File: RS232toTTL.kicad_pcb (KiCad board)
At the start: 2 copper layers, 48.5 x 32.5 mm, 15 parts, among them J1 DB9, P1 CONN_01X04, Q1 2N7002, Q2 PNP-BC857

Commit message: Routing PCB
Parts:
- moved R6 20.9 mm to (141.0, 103.5), turned to 180 degrees
- moved R7 19.1 mm to (141.0, 99.5), turned to 180 degrees
- moved D2 16.1 mm to (148.0, 103.5), turned to 180 degrees
- moved R2 15.7 mm to (138.0, 78.5), turned to 0 degrees
- moved R1 12.5 mm to (133.5, 78.5)
- moved D3 9.72 mm to (148.0, 99.5), turned to 180 degrees
- moved C1 7.28 mm to (137.5, 88.0), turned to 180 degrees
- moved P1 6.00 mm to (151.0, 88.0)
- moved D1 5.51 mm to (135.5, 82.0)
- moved Q1 5.45 mm to (145.9, 92.0), turned to 270 degrees
- moved Q2 4.61 mm to (133.5, 98.0)
- moved R5 4.00 mm to (133.5, 103.5), turned to 180 degrees
- moved R3 2.69 mm to (141.0, 96.5), turned to 0 degrees
- moved R4 2.06 mm to (134.0, 94.0)
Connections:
- P1 pad 1: VCC -> GND
- P1 pad 2: Net-(D2-Pad1) -> Net-(D3-Pad1)
- P1 pad 3: Net-(D3-Pad1) -> Net-(D2-Pad1)
- P1 pad 4: GND -> VCC
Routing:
- net Net-(D2-Pad1): track 0.00 -> 34.1 mm
- net VCC: track 0.00 -> 28.8 mm
- net Net-(D3-Pad1): track 0.00 -> 18.9 mm
- net Net-(Q1-Pad1): track 2.50 -> 19.8 mm
- net GND: track 0.00 -> 10.8 mm, vias 0 -> 2
- net Net-(Q2-Pad1): track 0.00 -> 10.5 mm, vias 0 -> 2
- net Net-(D1-Pad1): track 8.39 -> 16.9 mm
- net Net-(D3-Pad2): track 0.00 -> 5.10 mm
- net Net-(D2-Pad2): track 0.00 -> 5.10 mm
- net Net-(J1-Pad2): track 4.96 -> 9.42 mm
- net Net-(C1-Pad2): track 16.8 -> 13.6 mm
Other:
- board size 48.5 x 32.5 mm -> 43.5 x 32.5 mm
- net class 1mm added: clearance 0.3, trace_width 1, via_dia 2, via_drill 1
- net class Default: clearance 0.3 -> 0.5; via_dia 0.6 -> 2; via_drill 0.4 -> 1
- rule trace_clearance: 0.3 -> 0.5

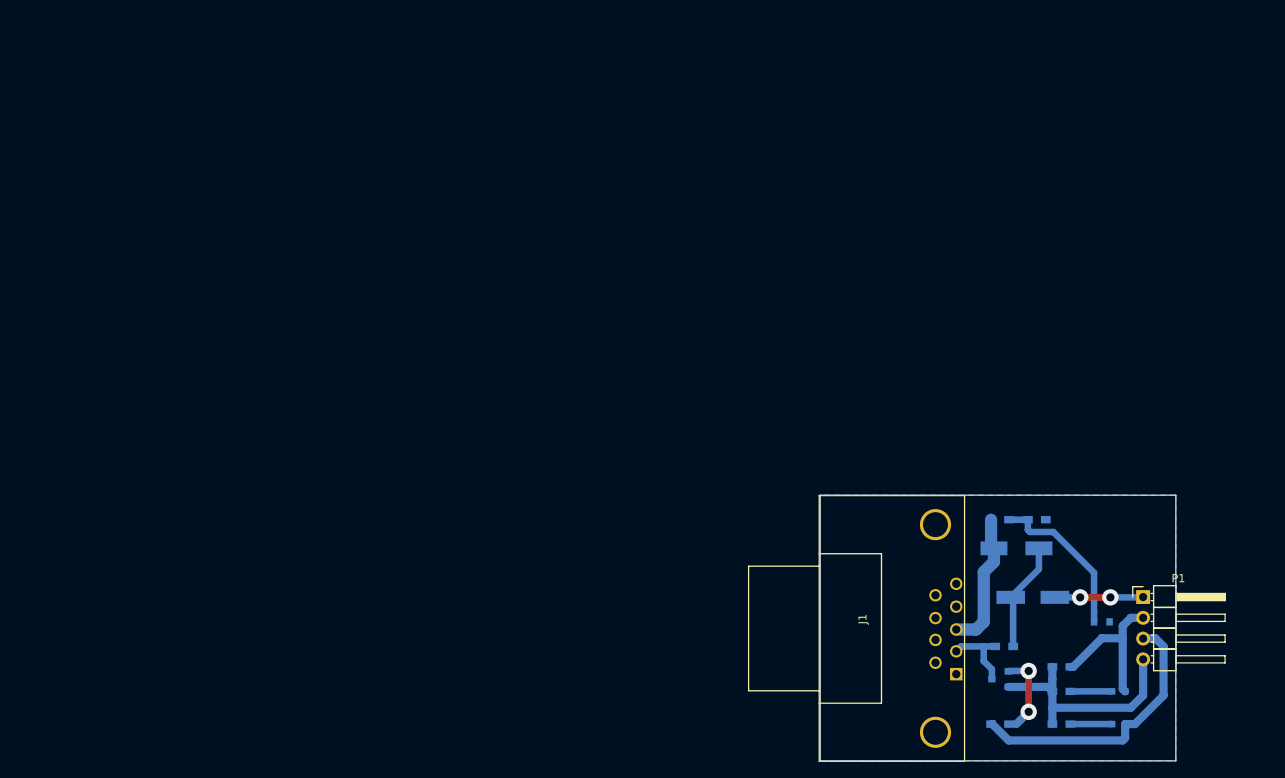
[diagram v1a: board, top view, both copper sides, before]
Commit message: Finalizing the PCB, first print successful
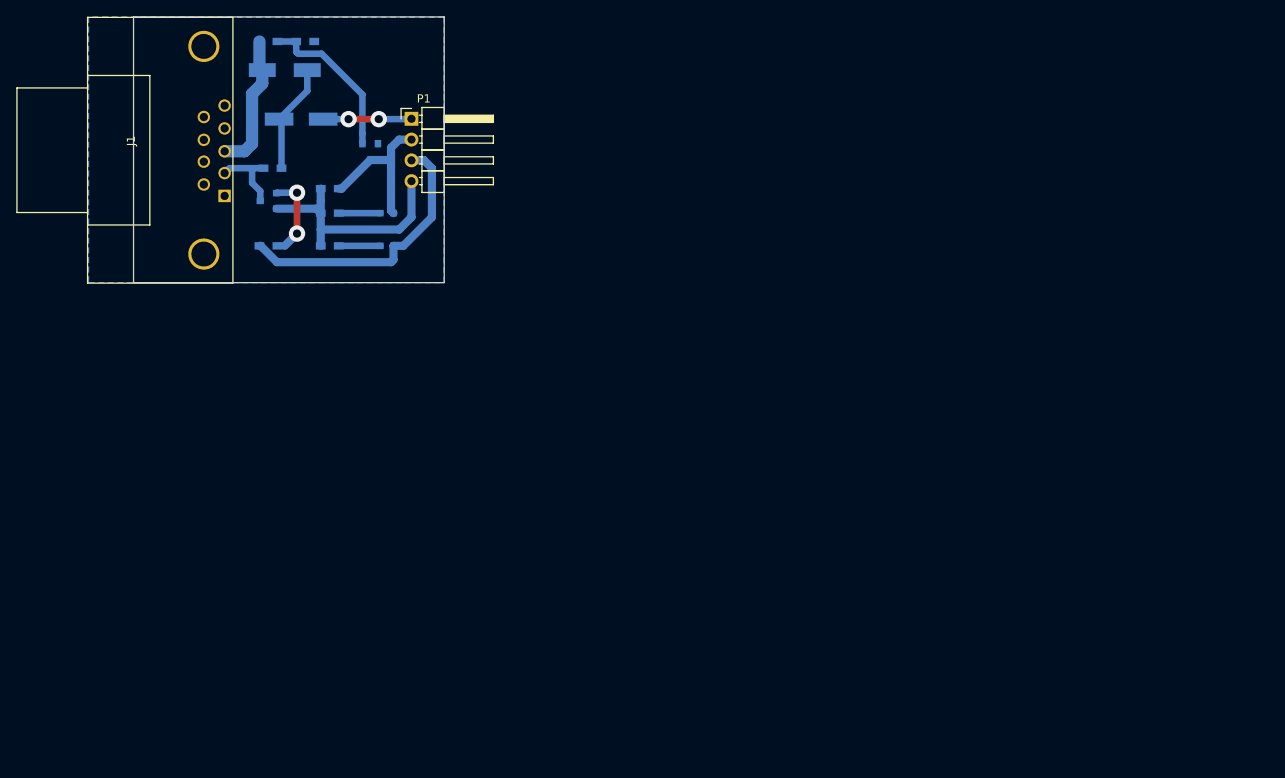
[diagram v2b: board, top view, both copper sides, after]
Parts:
- moved C1 106.9 mm to (48.0, 29.5)
- moved D1 106.9 mm to (46.0, 23.5)
- moved D2 106.9 mm to (58.5, 45.0)
- moved D3 106.9 mm to (58.5, 41.0)
- moved J1 106.9 mm to (37.4, 33.4)
- moved P1 106.9 mm to (61.5, 29.5)
- moved Q1 106.9 mm to (56.5, 33.5)
- moved Q2 106.9 mm to (44.0, 39.5)
- moved R1 106.9 mm to (44.0, 20.0)
- moved R2 106.9 mm to (48.5, 20.0)
- moved R3 106.9 mm to (51.5, 38.0)
- moved R4 106.9 mm to (44.5, 35.5)
- moved R5 106.9 mm to (44.0, 45.0)
- moved R6 106.9 mm to (51.5, 45.0)
- moved R7 106.9 mm to (51.5, 41.0)
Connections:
- J1 pad : (no net) -> GND
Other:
- board size 43.5 x 32.5 mm -> 38 x 32.5 mm
